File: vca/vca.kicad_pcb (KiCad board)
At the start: 2 copper layers, 68.6 x 101.6 mm, 27 parts, among them J1 Conn_01x02_Socket, J2 Conn_01x02_Socket, J3 Conn_01x02_Socket, J5 Conn_01x03_Socket, Q1 BC548C, Q2 BC548C, U1 TL074

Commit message: add vco remove zips
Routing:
- net Net-(U1B-+): track 31.2 -> 32.6 mm
- net GND: track 167.0 -> 168.1 mm
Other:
- board size 68.6 x 101.6 mm -> 70 x 100 mm
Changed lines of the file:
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@@
     )
   )
-  (gr_rect (start 76.916 22.352) (end 145.496 123.952)
+  (gr_rect (start 76.916 22.352) (end 146.916 122.352)
     (stroke (width 0.1) (type default)) (fill none) (layer "Edge.Cuts"))
   (segment (start 96.22 37.592) (end 93.5869 37.592) (width 0.25) (layer "B.Cu") (net 1))
@@
   (segment (start 92.5709 56.388) (end 94.0899 57.907) (width 0.25) (layer "B.Cu") (net 2))
   (segment (start 91.394 60.6029) (end 91.394 62.484) (width 0.25) (layer "B.Cu") (net 2))
-  (segment (start 121.9045 59.0339) (end 122.138 59.0339) (width 0.25) (layer "B.Cu") (net 2))
-  (segment (start 114.518 57.907) (end 118.9458 57.907) (width 0.25) (layer "B.Cu") (net 2))
   (segment (start 91.394 56.388) (end 92.5709 56.388) (width 0.25) (layer "B.Cu") (net 2))
-  (segment (start 120.9886 60.9924) (end 120.9886 59.9498) (width 0.25) (layer "B.Cu") (net 2))
-  (segment (start 122.138 61.8601) (end 121.8563 61.8601) (width 0.25) (layer "B.Cu") (net 2))
+  (segment (start 118.572 59.421) (end 122.138 62.987) (width 0.25) (layer "B.Cu") (net 2))
+  (segment (start 118.572 57.907) (end 118.572 59.421) (width 0.25) (layer "B.Cu") (net 2))
   (segment (start 106.1828 32.004) (end 97.0388 41.148) (width 0.25) (layer "B.Cu") (net 2))
-  (segment (start 122.138 62.4235) (end 122.138 61.8601) (width 0.25) (layer "B.Cu") (net 2))
   (segment (start 109.428 32.004) (end 106.1828 32.004) (width 0.25) (layer "B.Cu") (net 2))
   (segment (start 138.638 72.644) (end 132.3585 72.644) (width 0.25) (layer "B.Cu") (net 2))
   (segment (start 94.0899 57.907) (end 114.518 57.907) (width 0.25) (layer "B.Cu") (net 2))
-  (segment (start 121.8563 61.8601) (end 120.9886 60.9924) (width 0.25) (layer "B.Cu") (net 2))
-  (segment (start 120.9886 59.9498) (end 121.9045 59.0339) (width 0.25) (layer "B.Cu") (net 2))
+  (segment (start 118.572 57.907) (end 122.138 57.907) (width 0.25) (layer "B.Cu") (net 2))
   (segment (start 122.138 62.987) (end 122.138 62.4235) (width 0.25) (layer "B.Cu") (net 2))
   (segment (start 132.3585 72.644) (end 122.138 62.4235) (width 0.25) (layer "B.Cu") (net 2))
-  (segment (start 122.138 57.907) (end 122.138 59.0339) (width 0.25) (layer "B.Cu") (net 2))
   (segment (start 94.0899 57.907) (end 91.394 60.6029) (width 0.25) (layer "B.Cu") (net 2))
-  (segment (start 118.9458 57.907) (end 120.9886 59.9498) (width 0.25) (layer "B.Cu") (net 2))
+  (segment (start 114.518 57.907) (end 118.572 57.907) (width 0.25) (layer "B.Cu") (net 2))
   (segment (start 104.749 88.3629) (end 105.11 88.7239) (width 0.25) (layer "F.Cu") (net 3))
   (segment (start 105.11 88.7239) (end 105.11 90.932) (width 0.25) (layer "F.Cu") (net 3))
@@
   (segment (start 111.8687 43.1525) (end 112.984 44.2678) (width 0.25) (layer "B.Cu") (net 8))
   (segment (start 112.984 44.34) (end 113.9246 45.2806) (width 0.25) (layer "B.Cu") (net 8))
-  (segment (start 113.3911 46.3398) (end 114.508 45.2229) (width 0.25) (layer "F.Cu") (net 9))
-  (segment (start 113.8136 54.2401) (end 113.3911 53.8176) (width 0.25) (layer "F.Cu") (net 9))
-  (segment (start 114.518 55.367) (end 114.518 54.2401) (width 0.25) (layer "F.Cu") (net 9))
-  (segment (start 114.508 44.196) (end 114.508 45.2229) (width 0.25) (layer "F.Cu") (net 9))
-  (segment (start 114.518 54.2401) (end 113.8136 54.2401) (width 0.25) (layer "F.Cu") (net 9))
-  (segment (start 113.3911 53.8176) (end 113.3911 46.3398) (width 0.25) (layer "F.Cu") (net 9))
+  (segment (start 114.508 45.2229) (end 114.508 44.196) (width 0.25) (layer "F.Cu") (net 9))
+  (segment (start 112.9895 46.7414) (end 114.508 45.2229) (width 0.25) (layer "F.Cu") (net 9))
+  (segment (start 112.9895 54.2401) (end 112.9895 46.7414) (width 0.25) (layer "F.Cu") (net 9))
+  (segment (start 112.9895 54.2401) (end 113.3911 54.2401) (width 0.25) (layer "F.Cu") (net 9))
+  (segment (start 113.3911 54.2401) (end 114.518 55.367) (width 0.25) (layer "F.Cu") (net 9))
   (segment (start 112.0566 42.6825) (end 105.3535 42.6825) (width 0.25) (layer "B.Cu") (net 9))
   (segment (start 113.4811 44.107) (end 112.0566 42.6825) (width 0.25) (layer "B.Cu") (net 9))
@@
   (segment (start 114.508 72.644) (end 113.4804 73.6716) (width 0.25) (layer "F.Cu") (net 11))
   (segment (start 113.4804 91.9364) (end 114 92.456) (width 0.25) (layer "F.Cu") (net 11))
-  (segment (start 113.3754 71.5114) (end 114.508 72.644) (width 0.25) (layer "B.Cu") (net 11))
-  (segment (start 113.3754 64.9748) (end 113.3754 71.5114) (width 0.25) (layer "B.Cu") (net 11))
-  (segment (start 114.518 62.987) (end 114.518 64.1139) (width 0.25) (layer "B.Cu") (net 11))
-  (segment (start 114.2363 64.1139) (end 113.3754 64.9748) (width 0.25) (layer "B.Cu") (net 11))
-  (segment (start 114.518 64.1139) (end 114.2363 64.1139) (width 0.25) (layer "B.Cu") (net 11))
+  (segment (start 111.46 69.596) (end 114.508 72.644) (width 0.5) (layer "B.Cu") (net 11))
+  (segment (start 114.518 62.987) (end 111.465 66.04) (width 0.5) (layer "B.Cu") (net 11))
+  (segment (start 111.465 66.04) (end 111.46 66.04) (width 0.5) (layer "B.Cu") (net 11))
+  (segment (start 111.46 66.04) (end 111.46 69.596) (width 0.5) (layer "B.Cu") (net 11))
   (segment (start 114.518 66.6539) (end 114.7997 66.6539) (width 0.25) (layer "F.Cu") (net 12))
   (segment (start 115.6726 76.6337) (end 115.0903 77.216) (width 0.25) (layer "F.Cu") (net 12))
@@
   (segment (start 133.812 88.646) (end 133.812 95.504) (width 0.25) (layer "F.Cu") (net 14))
   (segment (start 114.518 59.3201) (end 114.3141 59.3201) (width 0.25) (layer "F.Cu") (net 15))
-  (segment (start 111.968 32.004) (end 111.968 33.1809) (width 0.25) (layer "F.Cu") (net 15))
-  (segment (start 112.5395 55.3085) (end 111.46 56.388) (width 0.25) (layer "F.Cu") (net 15))
-  (segment (start 112.5395 33.7524) (end 112.5395 55.3085) (width 0.25) (layer "F.Cu") (net 15))
+  (segment (start 111.968 46.228) (end 111.968 55.88) (width 0.25) (layer "F.Cu") (net 15))
+  (segment (start 111.968 46.228) (end 112.984 45.212) (width 0.25) (layer "F.Cu") (net 15))
+  (segment (start 112.984 42.672) (end 111.968 41.656) (width 0.25) (layer "F.Cu") (net 15))
+  (segment (start 111.968 55.88) (end 111.46 56.388) (width 0.25) (layer "F.Cu") (net 15))
+  (segment (start 112.984 45.212) (end 112.984 42.672) (width 0.25) (layer "F.Cu") (net 15))
   (segment (start 114.3141 59.3201) (end 111.46 56.466) (width 0.25) (layer "F.Cu") (net 15))
-  (segment (start 111.968 33.1809) (end 112.5395 33.7524) (width 0.25) (layer "F.Cu") (net 15))
+  (segment (start 111.968 32.004) (end 111.968 41.656) (width 0.25) (layer "F.Cu") (net 15))
   (segment (start 111.46 56.466) (end 111.46 56.388) (width 0.25) (layer "F.Cu") (net 15))
   (segment (start 114.518 60.447) (end 114.518 59.3201) (width 0.25) (layer "F.Cu") (net 15))

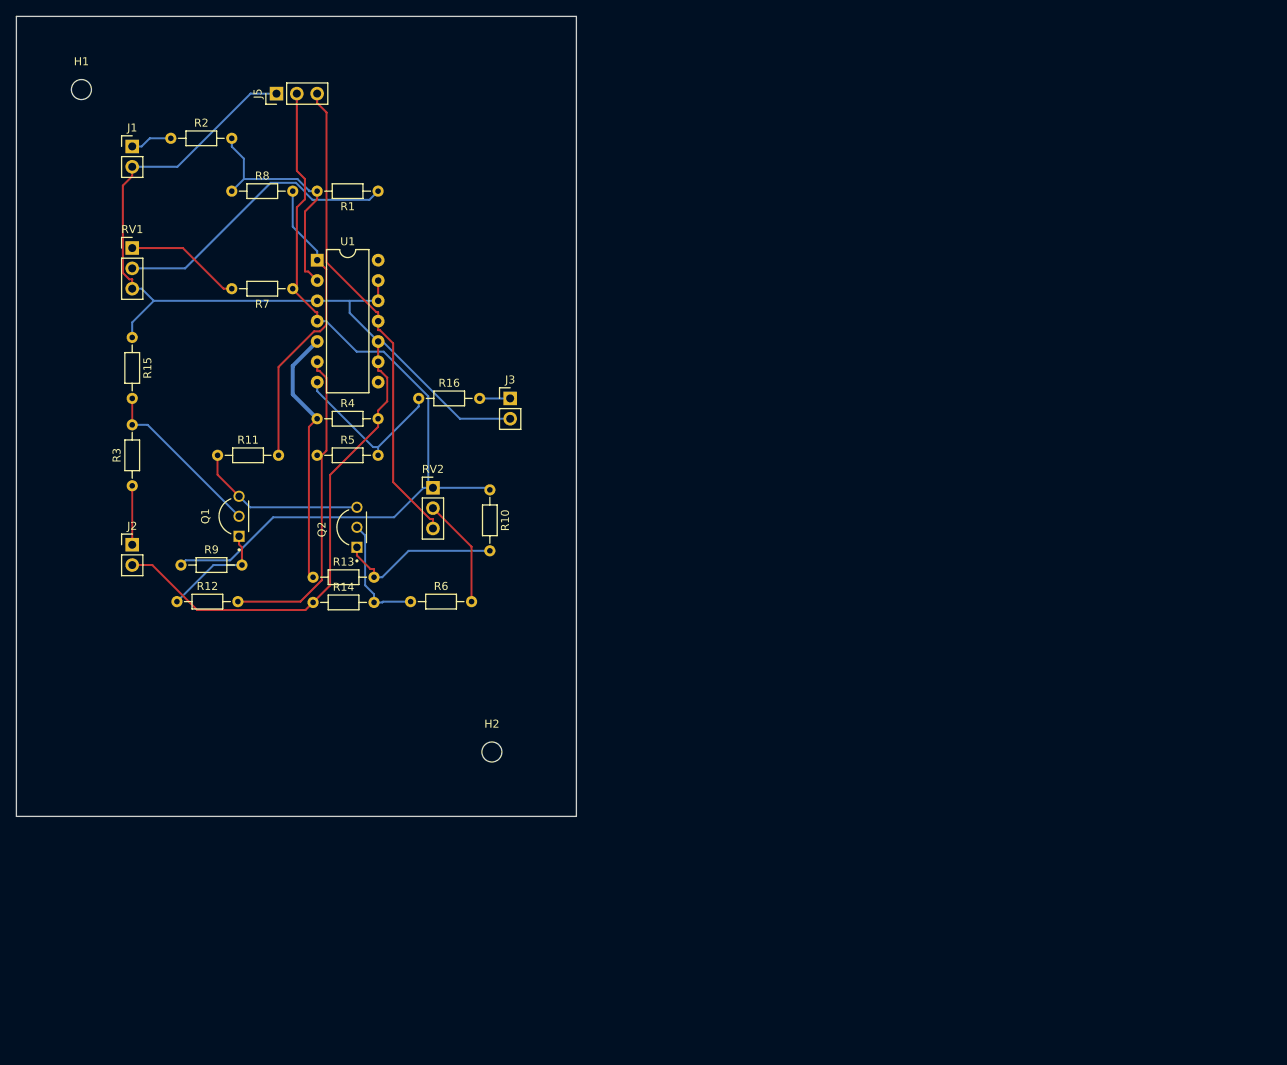
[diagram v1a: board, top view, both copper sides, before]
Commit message: add the eg and reroute the vca.
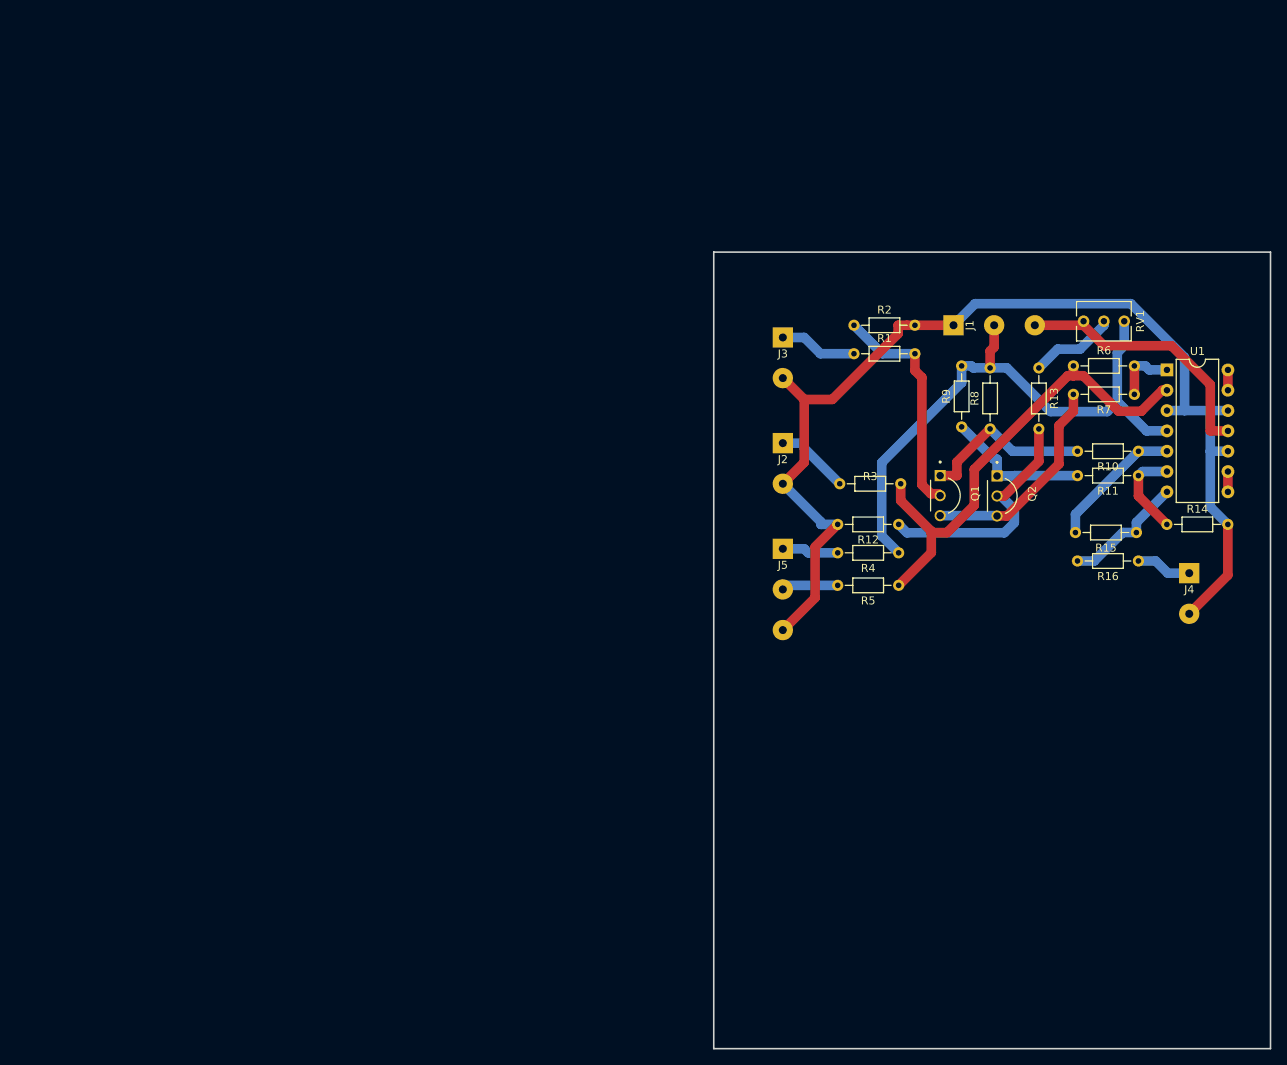
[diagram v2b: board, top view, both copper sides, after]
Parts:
- removed H1, H2: MountingHole, MountingHole:MountingHole_2.5mm
- removed RV2: 100K, Connector_PinHeader_2.54mm:PinHeader_1x03_P2.54mm_Vertical
- added J4: Conn_01x02_Socket, my_library:my_really_cool_2pin, F.Cu at (223.5, 94.5)
- J1: value Conn_01x02_Socket -> Conn_01x03_Socket; footprint Connector_PinHeader_2.54mm:PinHeader_1x02_P2.54mm_Vertical -> my_library:my_really_cool_3pin
- J2, J3: footprint Connector_PinHeader_2.54mm:PinHeader_1x02_P2.54mm_Vertical -> my_library:my_really_cool_2pin
- J5: footprint Connector_PinHeader_2.54mm:PinHeader_1x03_P2.54mm_Vertical -> my_library:my_really_cool_3pin
- R1, R3, R5: value 100K -> 100k
- R10, R7: value 20K -> 10k
- R11: value 10K -> 10k
- R12: value 10K -> 100
- R13: value 10K -> 100k
- R14, R15: value 100 -> 100k
- R16: value 1K -> 1k
- R2: value 100K -> 100
- R4: value 100K -> 20k
- R6: value 100K -> 82k
- R8: value 82K -> 20k
- R9: value 20K -> 20k
- RV1: value 100K -> 100k; footprint Connector_PinHeader_2.54mm:PinHeader_1x03_P2.54mm_Vertical -> Potentiometer_THT:Potentiometer_Vishay_T73XW_Horizontal
- moved R15 127.9 mm to (216.9, 86.9), turned to 180 degrees
- moved RV1 124.3 mm to (215.4, 60.5), turned to -90 degrees
- moved R11 115.1 mm to (217.2, 79.8), turned to 180 degrees
- moved J1 107.6 mm to (196.6, 61.0), turned to 90 degrees
- moved R14 107.2 mm to (220.7, 85.9)
- moved U1 107.1 mm to (220.7, 66.5)
- moved R7 106.0 mm to (216.7, 69.6)
- moved R8 99.3 mm to (198.6, 73.9), turned to 90 degrees
- moved R9 99.1 mm to (195.1, 73.7), turned to 90 degrees
- moved R13 94.4 mm to (204.7, 66.3), turned to -90 degrees
- moved R16 92.2 mm to (217.2, 90.4), turned to 180 degrees
- moved R12 90.7 mm to (187.2, 85.9), turned to 180 degrees
- moved Q1 89.0 mm to (193.0, 82.3), turned to -90 degrees
- moved R2 88.5 mm to (181.6, 61.0)
- moved R3 88.4 mm to (179.8, 80.8), turned to 0 degrees
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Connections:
- J1 pad 1: Net-(J1-Pin_1) -> GND
- J1 pad 2: GND -> +12V
- J5 pad 1: GND -> Net-(J5-Pin_1)
- J5 pad 2: +12V -> Net-(J5-Pin_2)
- J5 pad 3: -12V -> GND
- R1 pad 1: Net-(R1-Pad1) -> Net-(J3-Pin_1)
- R1 pad 2: Net-(U1A--) -> Net-(Q1-Pad2)
- R10 pad 1: +12V -> Net-(U1B-+)
- R10 pad 2: Net-(Q2-Pad1) -> Net-(Q1-Pad1)
- R11 pad 1: Net-(Q1-Pad3) -> Net-(U1B--)
- R11 pad 2: Net-(R11-Pad2) -> Net-(Q2-Pad1)
- R12 pad 1: Net-(Q1-Pad1) -> Net-(Q2-Pad2)
- R12 pad 2: Net-(U1B--) -> GND
- R13 pad 1: Net-(U1B-+) -> Net-(R13-Pad1)
- R13 pad 2: Net-(Q2-Pad1) -> Net-(Q2-Pad2)
- R14 pad 1: GND -> Net-(U1B--)
- R14 pad 2: Net-(Q2-Pad2) -> GND
- R15 pad 1: GND -> Net-(R15-Pad1)
- R15 pad 2: Net-(Q1-Pad2) -> Net-(U1B-+)
- R16 pad 1: Net-(R16-Pad1) -> Net-(J4-Pin_1)
- R16 pad 2: Net-(J3-Pin_1) -> Net-(R15-Pad1)
- R2 pad 1: Net-(J1-Pin_1) -> Net-(Q1-Pad2)
- R2 pad 2: Net-(U1A--) -> GND
- R3 pad 2: Net-(Q1-Pad2) -> Net-(U1A--)
- R4 pad 1: Net-(U1B-+) -> +12V
- R4 pad 2: GND -> Net-(J5-Pin_1)
- R5 pad 1: Net-(U1B--) -> Net-(U1A--)
- R5 pad 2: Net-(R16-Pad1) -> Net-(J5-Pin_2)
- R6 pad 1: Net-(Q2-Pad2) -> Net-(U1A--)
- R7 pad 1: +12V -> Net-(R6-Pad2)
- R7 pad 2: Net-(R7-Pad2) -> Net-(Q1-Pad3)
- R8 pad 1: Net-(U1A--) -> Net-(Q1-Pad1)
- R8 pad 2: Net-(R11-Pad2) -> +12V
- R9 pad 1: +12V -> Net-(Q2-Pad1)
- R9 pad 2: Net-(Q1-Pad1) -> +12V
- RV1 pad 1: Net-(R7-Pad2) -> +12V
- RV1 pad 2: Net-(R1-Pad1) -> Net-(R13-Pad1)
- RV1 pad 3: GND -> -12V
- U1 pad 1: Net-(R11-Pad2) -> Net-(R6-Pad2)
- U1 pad 13: GND -> Net-(U1D--)
- U1 pad 14: unconnected-(U1-Pad14) -> Net-(U1D--)
- U1 pad 7: Net-(R16-Pad1) -> Net-(R15-Pad1)
- U1 pad 8: unconnected-(U1-Pad8) -> Net-(U1C--)
- U1 pad 9: GND -> Net-(U1C--)
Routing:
- net Net-(R11-Pad2): track 37.7 -> 0.00 mm
- net Net-(R1-Pad1): track 36.5 -> 0.00 mm
- net Net-(U1A--): track 30.4 -> 60.3 mm
- net Net-(U1B--): track 40.4 -> 11.3 mm
- net +12V: track 102.8 -> 74.4 mm
- net -12V: track 60.8 -> 33.5 mm
- net GND: track 168.1 -> 141.3 mm
- net Net-(R16-Pad1): track 20.9 -> 0.00 mm
- net Net-(Q2-Pad2): track 14.9 -> 31.0 mm
- net Net-(U1B-+): track 32.6 -> 17.0 mm
- net Net-(R15-Pad1): track 0.00 -> 15.5 mm
- net Net-(R7-Pad2): track 14.6 -> 0.00 mm
- net Net-(R13-Pad1): track 0.00 -> 10.9 mm
- net Net-(Q1-Pad1): track 13.8 -> 21.7 mm
- net Net-(Q1-Pad2): track 21.4 -> 28.7 mm
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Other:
- board size 70 x 100 mm -> 69.6 x 99.6 mm
